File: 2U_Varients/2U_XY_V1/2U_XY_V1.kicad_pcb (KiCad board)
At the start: 4 copper layers, 83 x 213 mm, 31 parts, among them CN1 DF11-2DSA-4DP, J2 Conn_01x01, J3 Conn_01x01, J4 Conn_01x01, J5 Conn_01x01, U2 TMP112xxDRL, U3 DRV2605LDGS, U4 TCA4311ADGKR, U5 5040500691, U6 5040500691, U7 VEML6031X00

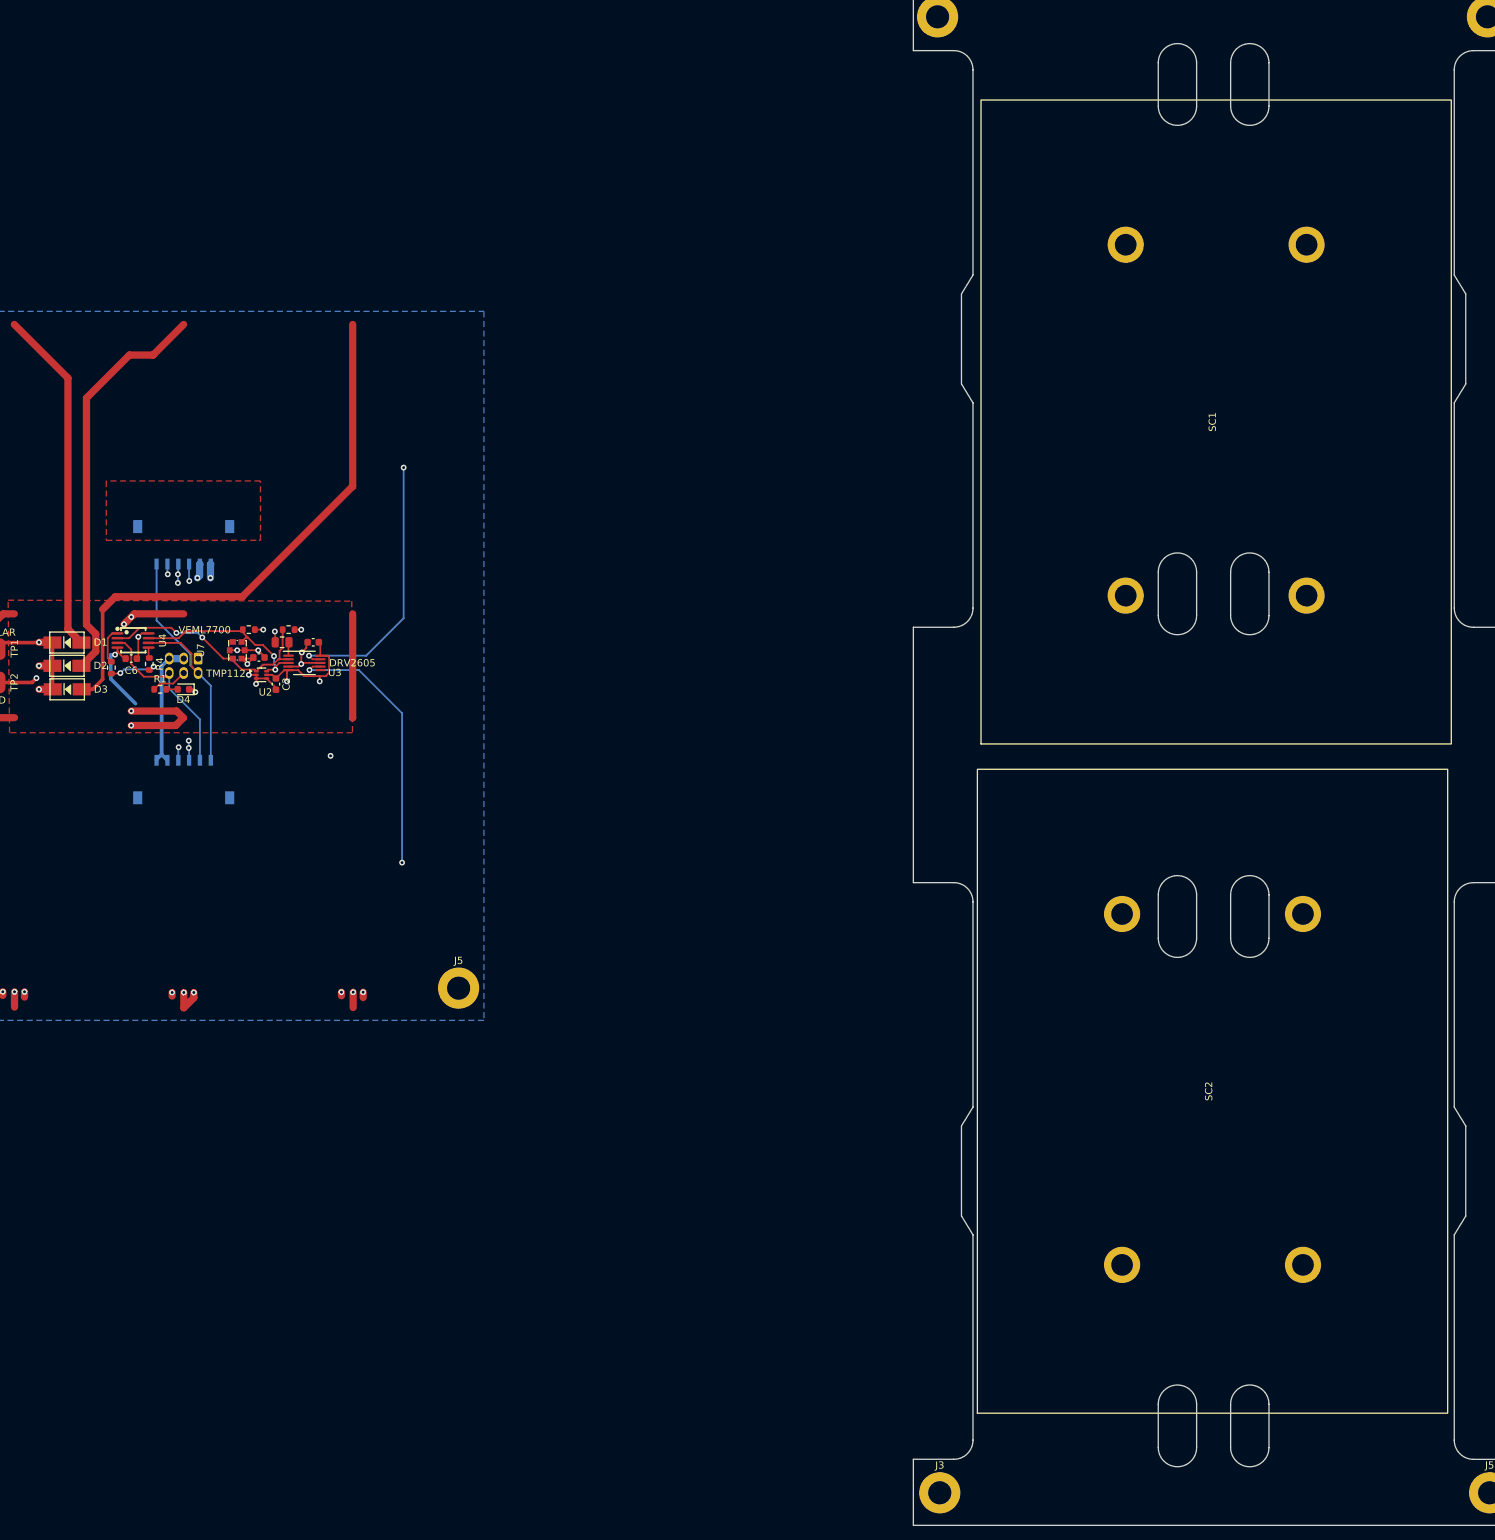
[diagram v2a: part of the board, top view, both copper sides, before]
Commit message: Moved Components into the Spot
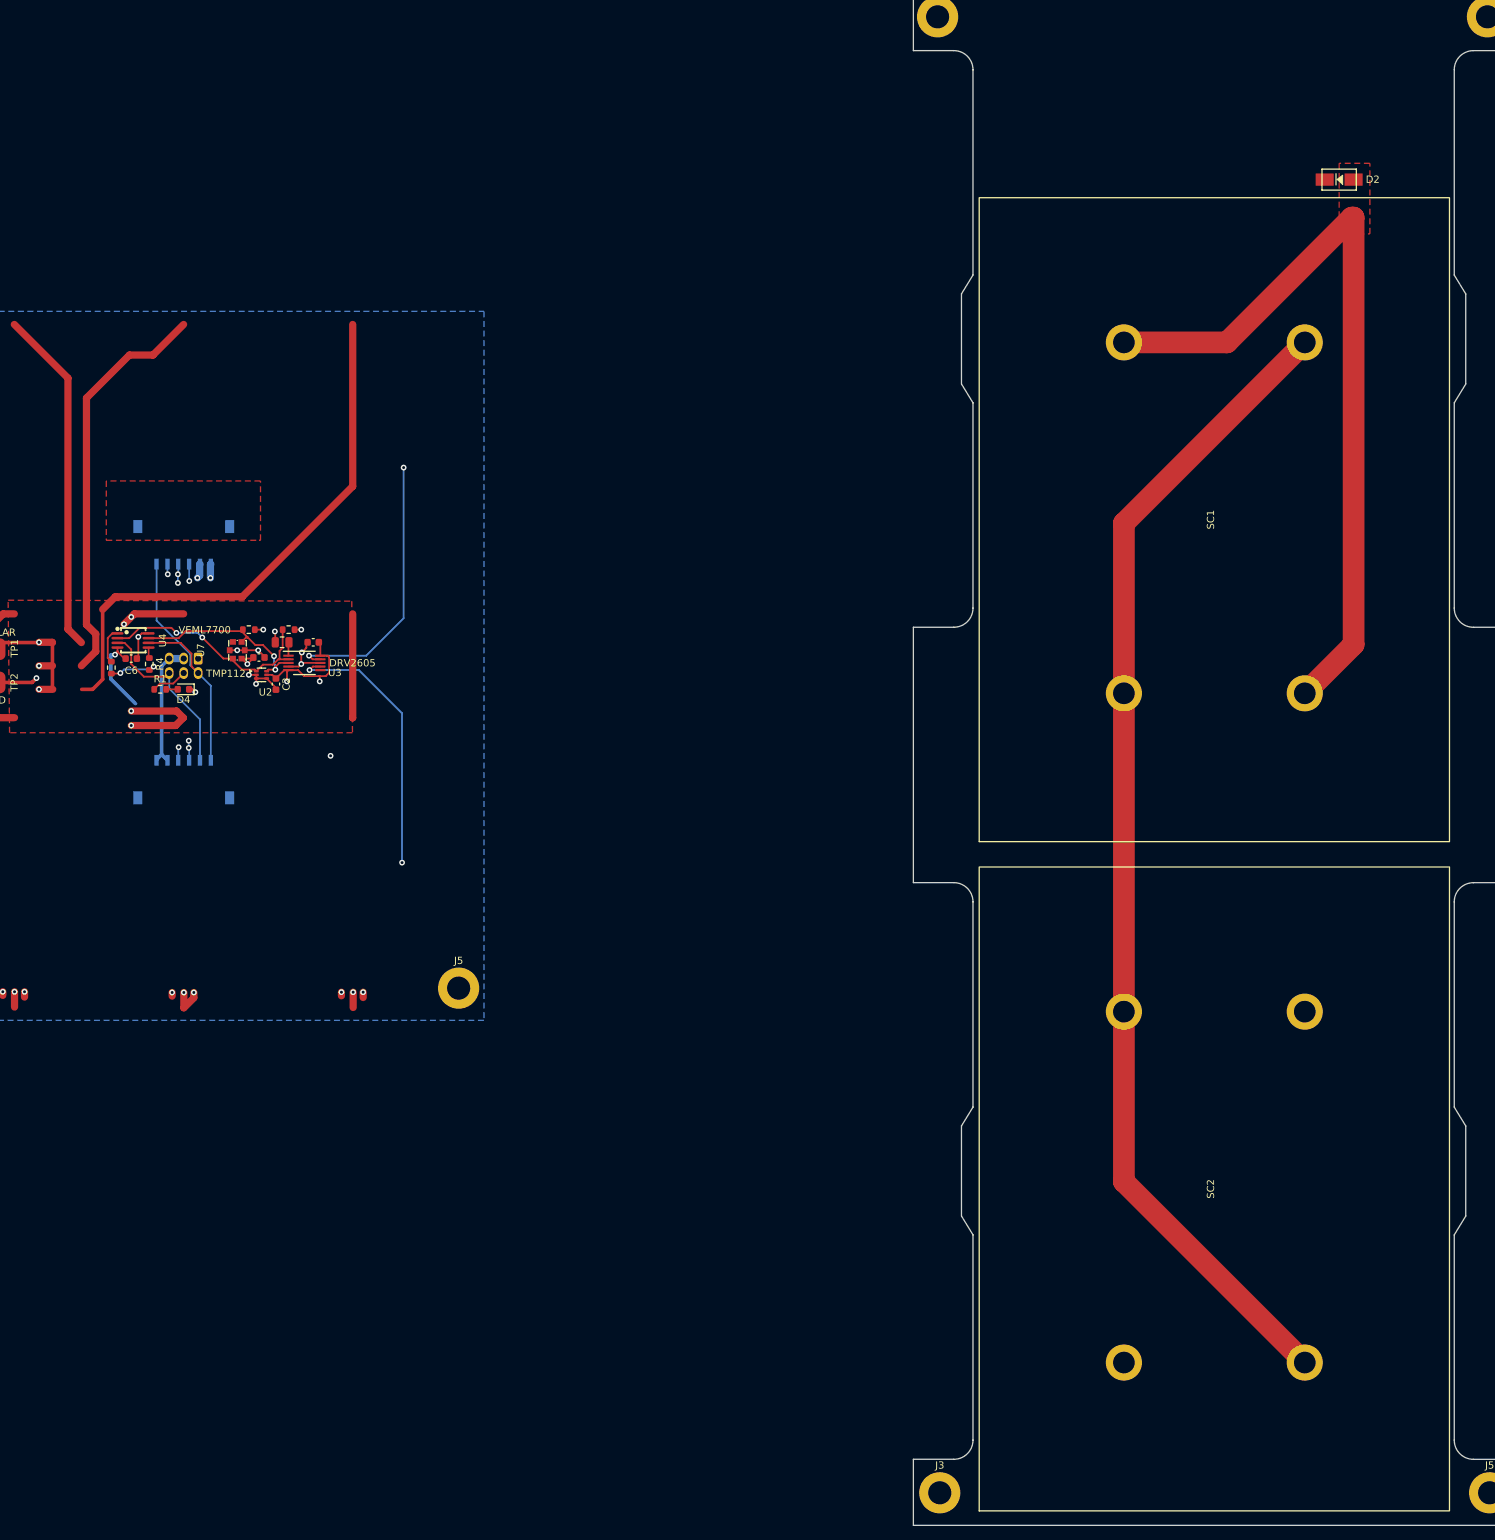
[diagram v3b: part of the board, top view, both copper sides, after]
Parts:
- removed D1, D3: CDBA240LL-HF, SolarPanelBoards:DO-214AC
- moved D2 188.2 mm to (227.0, 63.0)
- moved SC1 13.5 mm to (222.2, 85.5)
- moved SC2 13.5 mm to (222.2, 178.0)
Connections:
- net Net-(D2-A) renamed /SOL_OUT
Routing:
- net (no net): track 75.4 -> 256.4 mm
- net Net-(SC1---Pad2): track 0.00 -> 161.7 mm
- net Net-(D3-A): track 77.1 -> 0.00 mm
- net /SOL_OUT: track 56.0 -> 107.4 mm
- net Net-(D1-A): track 47.8 -> 0.00 mm
- added copper zone on F.Cu, net /SOL_OUT
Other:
- outline, holes or cut-outs redrawn

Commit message: Expanded Coils to 2U
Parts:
- removed the J3 at (29.3, 174.8)
- removed the J5 at (105.3, 174.8)
- moved U5 227.8 mm to (-149.2, 216.6)
- moved U6 227.8 mm to (-149.2, 184.3)
- moved D4 162.6 mm to (208.6, 53.0)
- moved R1 162.6 mm to (205.4, 53.0)
- moved CN1 159.5 mm to (211.0, 56.0)
- moved U3 158.9 mm to (222.3, 51.7)
- moved U7 158.9 mm to (213.1, 50.0)
- moved C2 158.9 mm to (218.4, 54.6)
- moved C3 158.9 mm to (223.6, 48.9)
- moved C5 158.9 mm to (219.2, 48.9)
- moved C6 158.9 mm to (198.4, 51.1)
- moved R2 158.9 mm to (195.7, 52.4)
- moved R4 158.9 mm to (200.9, 51.9)
- moved R5 158.9 mm to (220.2, 47.1)
- moved R6 158.9 mm to (214.7, 47.1)
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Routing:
- net Net-(U3-OUT+): track 9246.2 -> 20444.7 mm
- net (no net): track 256.4 -> 0.00 mm, vias 4 -> 0
- net VSOLAR: track 88.8 -> 1.29 mm, vias 5 -> 0
- net +3V3: track 110.7 -> 63.2 mm, vias 12 -> 8
- net SCLIN: track 45.7 -> 0.00 mm, vias 1 -> 0
- net SDAIN: track 39.8 -> 0.00 mm
- net GND: track 55.0 -> 23.4 mm, vias 21 -> 8
- net /SCL: track 32.0 -> 26.5 mm
- removed copper zone on F.Cu, net +3V3
- removed copper zone on In2.Cu, net +3V3

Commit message: Placed the Driver
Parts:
- removed U6: 5040500691, easyeda2kicad:CONN-SMD_6P-P1.50_A1501WRB-S-6P
- C2, C3, C4, C5, C6, R1, R2, R4, R5, R6, U3, U4: moved to B.Cu
- moved U5 387.9 mm to (209.0, 67.8)
- moved R5 16.3 mm to (204.6, 51.8), turned to 180 degrees
- moved C6 15.2 mm to (213.6, 51.6), turned to 180 degrees
- moved R4 14.5 mm to (215.1, 48.9), turned to 0 degrees
- moved C3 14.3 mm to (214.9, 60.3), turned to 90 degrees
- moved C2 11.7 mm to (209.0, 47.8), turned to 0 degrees
- moved U4 10.6 mm to (209.1, 50.5), turned to 90 degrees
- moved R2 10.2 mm to (205.8, 53.3), turned to 0 degrees
- moved U3 8.67 mm to (217.8, 59.1), turned to -90 degrees
- moved U2 8.50 mm to (209.0, 49.2)
- moved C5 8.35 mm to (214.9, 56.0), turned to 90 degrees
- moved U7 4.49 mm to (209.0, 51.9)
- moved CN1 4.48 mm to (207.0, 58.0), turned to 0 degrees
- moved R1 3.67 mm to (209.0, 53.3), turned to 180 degrees
- moved C4 3.32 mm to (213.6, 53.1)
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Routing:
- net VSOLAR: track 1.29 -> 55.9 mm, vias 0 -> 3
- net +3V3: track 63.2 -> 36.3 mm, vias 8 -> 12
- net SCLIN: track 0.00 -> 25.1 mm, vias 0 -> 1
- net SDAIN: track 0.00 -> 23.2 mm
- net /SDA: track 26.0 -> 19.1 mm, vias 2 -> 1
- net Net-(U4-EN): track 5.09 -> 1.89 mm
- net GND: track 23.4 -> 25.8 mm, vias 8 -> 10
- net Net-(U4-READY): track 1.49 -> 3.37 mm
- net Net-(D4-A): track 1.60 -> 2.13 mm, vias 0 -> 1
- added copper zone on In2.Cu, net +3V3
- added copper zone on In1.Cu, net VSOLAR

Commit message: 2U V1: As Ordered October 9, 2025
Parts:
- added G***: LOGO, LOGO, B.Cu at (210.0, 108.5)
- added J112: Conn_01x01, MountingHole:MountingHole_3.2mm_M3_ISO7380_Pad, F.Cu at (171.8, 129.7)
- added J114: Conn_01x01, MountingHole:MountingHole_3.2mm_M3_ISO7380_Pad, F.Cu at (247.8, 129.7)
- added J12: Conn_01x01, MountingHole:MountingHole_3.2mm_M3_ISO7380_Pad, F.Cu at (171.8, 155.4)
- added J14: Conn_01x01, MountingHole:MountingHole_3.2mm_M3_ISO7380_Pad, F.Cu at (247.8, 155.4)
- C2: moved to F.Cu
- moved R6 4.99 mm to (217.2, 51.1), turned to 0 degrees
- moved R4 0.59 mm to (215.1, 49.5)
- moved J2 0.34 mm to (171.8, 40.6)
- moved J4 0.34 mm to (247.8, 40.6)
- moved C2 0.29 mm to (209.0, 47.5)
- moved J3 0.05 mm to (171.8, 244.4)
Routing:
- net Net-(U3-OUT+): track 20444.7 -> 20586.7 mm, vias 5 -> 3
- net GND: track 25.8 -> 26.8 mm, vias 10 -> 11
- net /SDA: track 19.1 -> 18.2 mm
- net +3V3: track 36.3 -> 35.5 mm
- added copper zone on B.Cu, net (none)
- removed copper zone on F.Cu, net (none)
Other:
- board size 83 x 213 mm -> 83 x 212.6 mm
- board text added: "+"
- board text added: "-"
- board text added: "Hi My Name Is Jimmy"
- board text added: "V1 2U Solar Panel Designed By: Michael Pham Reviewed By: William Hsu"
- board text removed: "PROVES XY SOLAR: KIT V3 AMANDA EWING, NICOLE MAGGARD Rachel Rakushkin, Michael Pham"
- board text removed: "TMP112"
- board text removed: "The PROVES Kit V3"
- board text removed: "VEML7700"
